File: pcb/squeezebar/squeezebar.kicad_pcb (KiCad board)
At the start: 2 copper layers, 104.1 x 20.3 mm, 55 parts, among them J2 Conn_02x08_Counter_Clockwise, U1 Elite-C

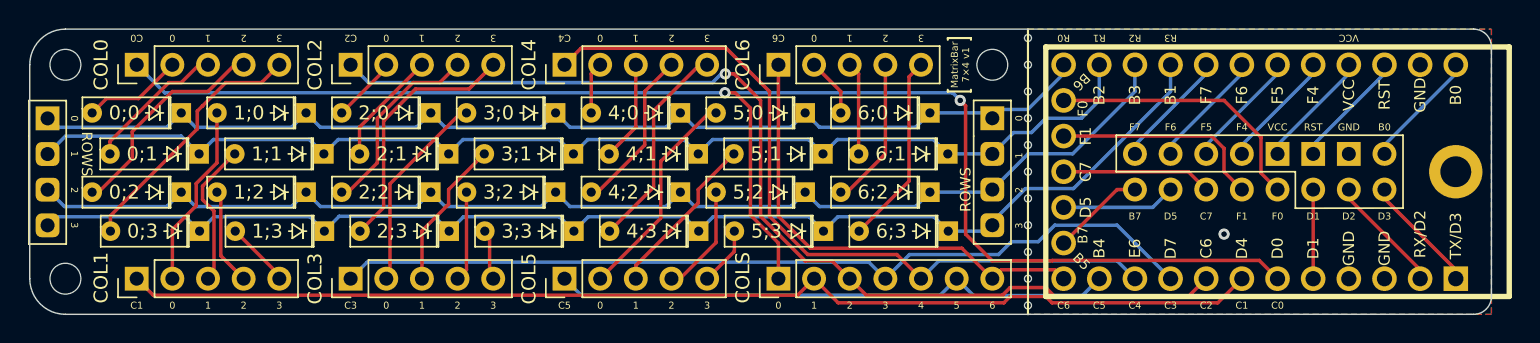
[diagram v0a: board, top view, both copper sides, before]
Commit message: Switch to M3 screws
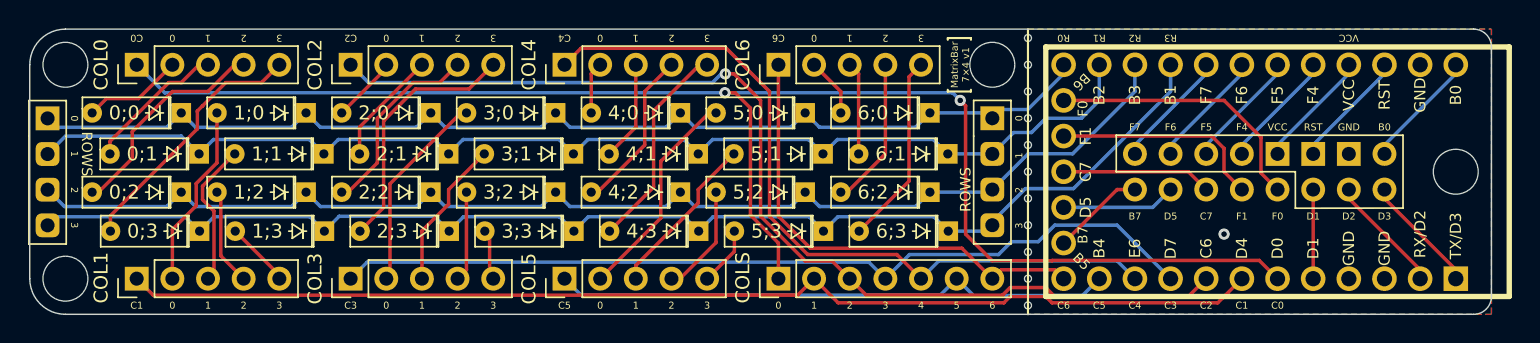
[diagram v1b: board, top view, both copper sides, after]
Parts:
- H1: footprint MountingHole:MountingHole_2.2mm_M2_DIN965_Pad -> MountingHole:MountingHole_3.2mm_M3_DIN965
- H2, H3, H4: footprint MountingHole:MountingHole_2.2mm_M2_DIN965 -> MountingHole:MountingHole_3.2mm_M3_DIN965
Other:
- board text added: "M3"
- board text removed: "M2"
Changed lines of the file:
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@@
   (net 54 "/pf1")
   (net 55 "/pf0")
-  (footprint "MountingHole:MountingHole_2.2mm_M2_DIN965" (layer "F.Cu")
+  (footprint "MountingHole:MountingHole_3.2mm_M3_DIN965" (layer "F.Cu")
     (at 30.48 60.96)
-    (descr "Mounting Hole 2.2mm, no annular, M2, DIN965")
-    (tags "mounting hole 2.2mm no annular m2 din965")
+    (descr "Mounting Hole 3.2mm, no annular, M3, DIN965")
+    (tags "mounting hole 3.2mm no annular m3 din965")
     (property "Sheetfile" "squeezebar.kicad_sch")
     (property "Sheetname" "")
     (attr exclude_from_pos_files)
-    (fp_text reference "H3" (at 0 -2.9) (layer "F.SilkS") hide
+    (fp_text reference "H3" (at 0 -3.8) (layer "F.SilkS") hide
       (effects (font (size 1 1) (thickness 0.15)))
     )
-    (fp_text value "MountingHole" (at 0 2.9) (layer "F.Fab")
+    (fp_text value "MountingHole" (at 0 3.8) (layer "F.Fab")
       (effects (font (size 1 1) (thickness 0.15)))
     )
@@
       (effects (font (size 1 1) (thickness 0.15)))
     )
-    (fp_circle (center 0 0) (end 1.9 0) (layer "Cmts.User") (width 0.15) (fill none))
-    (fp_circle (center 0 0) (end 2.15 0) (layer "F.CrtYd") (width 0.05) (fill none))
-    (pad "" np_thru_hole circle (at 0 0) (size 2.2 2.2) (drill 2.2) (layers *.Cu *.Mask))
+    (fp_circle (center 0 0) (end 2.8 0) (layer "Cmts.User") (width 0.15) (fill none))
+    (fp_circle (center 0 0) (end 3.05 0) (layer "F.CrtYd") (width 0.05) (fill none))
+    (pad "" np_thru_hole circle (at 0 0) (size 3.2 3.2) (drill 3.2) (layers *.Cu *.Mask))
   )
   (footprint "Library:breakaway-hole" (layer "F.Cu")
@@
       (net 26 "Net-(4;0-Pad2)") (pinfunction "A") (pintype "passive"))
   )
-  (footprint "MountingHole:MountingHole_2.2mm_M2_DIN965_Pad" (layer "F.Cu")
+  (footprint "MountingHole:MountingHole_3.2mm_M3_DIN965" (layer "F.Cu")
     (at 129.54 68.58)
-    (descr "Mounting Hole 2.2mm, M2, DIN965")
-    (tags "mounting hole 2.2mm m2 din965")
+    (descr "Mounting Hole 3.2mm, no annular, M3, DIN965")
+    (tags "mounting hole 3.2mm no annular m3 din965")
     (property "Sheetfile" "squeezebar.kicad_sch")
     (property "Sheetname" "")
     (attr exclude_from_pos_files)
-    (fp_text reference "H1" (at 0 -2.9) (layer "F.SilkS") hide
+    (fp_text reference "H1" (at 0 -3.8) (layer "F.SilkS") hide
       (effects (font (size 1 1) (thickness 0.15)))
     )
-    (fp_text value "MountingHole" (at 0 2.9) (layer "F.Fab")
+    (fp_text value "MountingHole" (at 0 3.8) (layer "F.Fab")
       (effects (font (size 1 1) (thickness 0.15)))
     )
@@
       (effects (font (size 1 1) (thickness 0.15)))
     )
-    (fp_circle (center 0 0) (end 1.9 0) (layer "Cmts.User") (width 0.15) (fill none))
-    (fp_circle (center 0 0) (end 2.15 0) (layer "F.CrtYd") (width 0.05) (fill none))
-    (pad "1" thru_hole circle (at 0 0) (size 3.8 3.8) (drill 2.2) (layers *.Cu *.Mask)
-      (net 40 "/gnd") (pinfunction "1") (pintype "input"))
+    (fp_circle (center 0 0) (end 2.8 0) (layer "Cmts.User") (width 0.15) (fill none))
+    (fp_circle (center 0 0) (end 3.05 0) (layer "F.CrtYd") (width 0.05) (fill none))
+    (pad "" np_thru_hole circle (at 0 0) (size 3.2 3.2) (drill 3.2) (layers *.Cu *.Mask))
   )
   (footprint "Library:PinHeader_1x05_P2.54mm_Vertical" (layer "F.Cu")
@@
       (net 5 "Net-(0;2-Pad2)") (pinfunction "A") (pintype "passive"))
   )
-  (footprint "MountingHole:MountingHole_2.2mm_M2_DIN965" (layer "F.Cu")
+  (footprint "MountingHole:MountingHole_3.2mm_M3_DIN965" (layer "F.Cu")
     (at 30.48 76.2)
-    (descr "Mounting Hole 2.2mm, no annular, M2, DIN965")
-    (tags "mounting hole 2.2mm no annular m2 din965")
+    (descr "Mounting Hole 3.2mm, no annular, M3, DIN965")
+    (tags "mounting hole 3.2mm no annular m3 din965")
     (property "Sheetfile" "squeezebar.kicad_sch")
     (property "Sheetname" "")
     (attr exclude_from_pos_files)
-    (fp_text reference "H4" (at 0 -2.9) (layer "F.SilkS") hide
+    (fp_text reference "H4" (at 0 -3.8) (layer "F.SilkS") hide
       (effects (font (size 1 1) (thickness 0.15)))
     )
-    (fp_text value "MountingHole" (at 0 2.9) (layer "F.Fab")
+    (fp_text value "MountingHole" (at 0 3.8) (layer "F.Fab")
       (effects (font (size 1 1) (thickness 0.15)))
     )
@@
       (effects (font (size 1 1) (thickness 0.15)))
     )
-    (fp_circle (center 0 0) (end 1.9 0) (layer "Cmts.User") (width 0.15) (fill none))
-    (fp_circle (center 0 0) (end 2.15 0) (layer "F.CrtYd") (width 0.05) (fill none))
-    (pad "" np_thru_hole circle (at 0 0) (size 2.2 2.2) (drill 2.2) (layers *.Cu *.Mask))
+    (fp_circle (center 0 0) (end 2.8 0) (layer "Cmts.User") (width 0.15) (fill none))
+    (fp_circle (center 0 0) (end 3.05 0) (layer "F.CrtYd") (width 0.05) (fill none))
+    (pad "" np_thru_hole circle (at 0 0) (size 3.2 3.2) (drill 3.2) (layers *.Cu *.Mask))
   )
   (footprint "Library:breakaway-hole" (layer "F.Cu")
@@
     )
   )
-  (footprint "MountingHole:MountingHole_2.2mm_M2_DIN965" (layer "F.Cu")
+  (footprint "MountingHole:MountingHole_3.2mm_M3_DIN965" (layer "F.Cu")
     (at 96.52 60.96)
-    (descr "Mounting Hole 2.2mm, no annular, M2, DIN965")
-    (tags "mounting hole 2.2mm no annular m2 din965")
+    (descr "Mounting Hole 3.2mm, no annular, M3, DIN965")
+    (tags "mounting hole 3.2mm no annular m3 din965")
     (property "Sheetfile" "squeezebar.kicad_sch")
     (property "Sheetname" "")
     (attr exclude_from_pos_files)
-    (fp_text reference "H2" (at 0 -2.9) (layer "F.SilkS") hide
+    (fp_text reference "H2" (at 0 -3.8) (layer "F.SilkS") hide
       (effects (font (size 1 1) (thickness 0.15)))
     )
-    (fp_text value "MountingHole" (at 0 2.9) (layer "F.Fab")
+    (fp_text value "MountingHole" (at 0 3.8) (layer "F.Fab")
       (effects (font (size 1 1) (thickness 0.15)))
     )
@@
       (effects (font (size 1 1) (thickness 0.15)))
     )
-    (fp_circle (center 0 0) (end 1.9 0) (layer "Cmts.User") (width 0.15) (fill none))
-    (fp_circle (center 0 0) (end 2.15 0) (layer "F.CrtYd") (width 0.05) (fill none))
-    (pad "" np_thru_hole circle (at 0 0) (size 2.2 2.2) (drill 2.2) (layers *.Cu *.Mask))
+    (fp_circle (center 0 0) (end 2.8 0) (layer "Cmts.User") (width 0.15) (fill none))
+    (fp_circle (center 0 0) (end 3.05 0) (layer "F.CrtYd") (width 0.05) (fill none))
+    (pad "" np_thru_hole circle (at 0 0) (size 3.2 3.2) (drill 3.2) (layers *.Cu *.Mask))
   )
   (footprint "Library:Diode" (layer "F.Cu")
@@
     (effects (font (size 0.5 0.5) (thickness 0.125)) (justify mirror))
   )
-  (gr_text "M2" (at 29.21 77.47 315) (layer "B.SilkS")
+  (gr_text "M3" (at 29.083 77.597 315) (layer "B.SilkS")
     (effects (font (size 0.5 0.5) (thickness 0.125)) (justify mirror))
   )
@@
     (effects (font (size 0.5 0.5) (thickness 0.125)))
   )
-  (dimension (type aligned) (layer "B.SilkS")
-    (pts (xy 30.48 76.2) (xy 27.94 76.2))
-    (height 1.27)
-    (gr_text "2.54" (at 29.21 74.93) (layer "B.SilkS")
-      (effects (font (size 0.5 0.5) (thickness 0.15)) (justify mirror))
-    )
-    (format (units 3) (units_format 0) (precision 2))
-    (style (thickness 0.15) (arrow_length 0.4) (text_position_mode 1) (extension_height 0.58642) (extension_offset 0.5) keep_text_aligned)
-  )
-  (dimension (type aligned) (layer "B.SilkS")
-    (pts (xy 30.48 76.2) (xy 30.48 78.74))
-    (height -1.27)
-    (gr_text "2.54" (at 31.75 77.47 90) (layer "B.SilkS")
-      (effects (font (size 0.5 0.5) (thickness 0.15)) (justify mirror))
-    )
-    (format (units 3) (units_format 0) (precision 2))
-    (style (thickness 0.15) (arrow_length 0.3) (text_position_mode 1) (extension_height 0.58642) (extension_offset 0.5) keep_text_aligned)
-  )
   (dimension (type aligned) (layer "Cmts.User")
     (pts (xy 27.88 66.05) (xy 134.874 66.04))
@@
   )
   (dimension (type aligned) (layer "User.1")
-    (pts (xy 129.54 68.58) (xy 129.54 66.548))
-    (height 7.62)
-    (gr_text "2 mm" (at 137.16 64.0334 90) (layer "User.1")
-      (effects (font (size 1 1) (thickness 0.15)))
-    )
-    (format (units 3) (units_format 1) (precision 1) suppress_zeroes)
-    (style (thickness 0.15) (arrow_length 1) (text_position_mode 2) (extension_height 0.58642) (extension_offset 0.5) keep_text_aligned)
-  )
-  (dimension (type aligned) (layer "User.1")
-    (pts (xy 27.94 78.74) (xy 97.155 78.74))
+    (pts (xy 27.94 78.74) (xy 96.52 78.74))
     (height 6.35)
-    (gr_text "69.22 mm" (at 62.5475 85.09) (layer "User.1")
+    (gr_text "68.58 mm" (at 62.23 85.09) (layer "User.1")
       (effects (font (size 1 1) (thickness 0.15)))
     )
@@
   )
   (dimension (type aligned) (layer "User.1")
-    (pts (xy 97.155 78.74) (xy 134.62 78.74))
+    (pts (xy 96.52 78.74) (xy 134.62 78.74))
     (height 6.35)
-    (gr_text "37.47 mm" (at 115.8875 85.09) (layer "User.1")
+    (gr_text "38.10 mm" (at 115.57 85.09) (layer "User.1")
       (effects (font (size 1 1) (thickness 0.15)))
     )

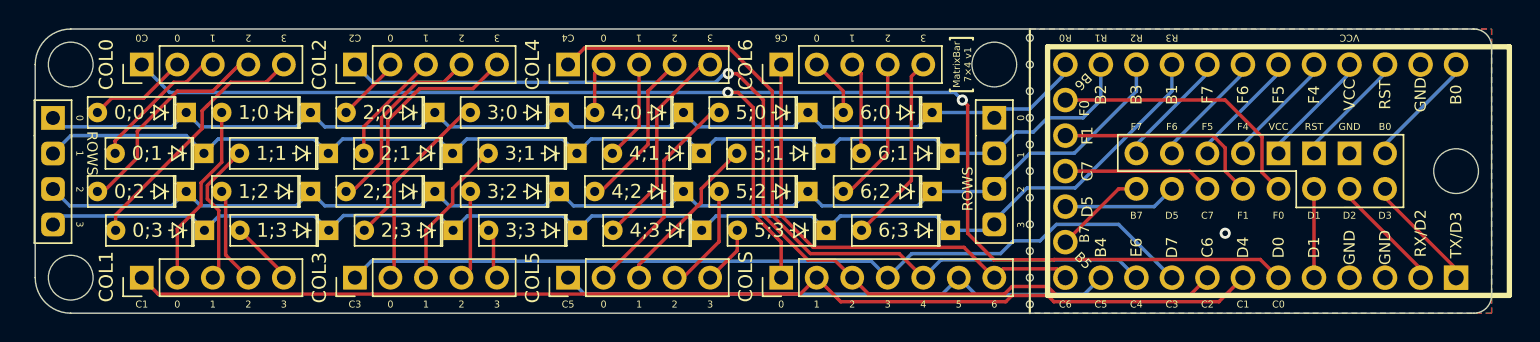
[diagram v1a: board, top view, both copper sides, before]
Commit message: Reassign pins; break out I²C & RST at the expense of 2 mounting holes
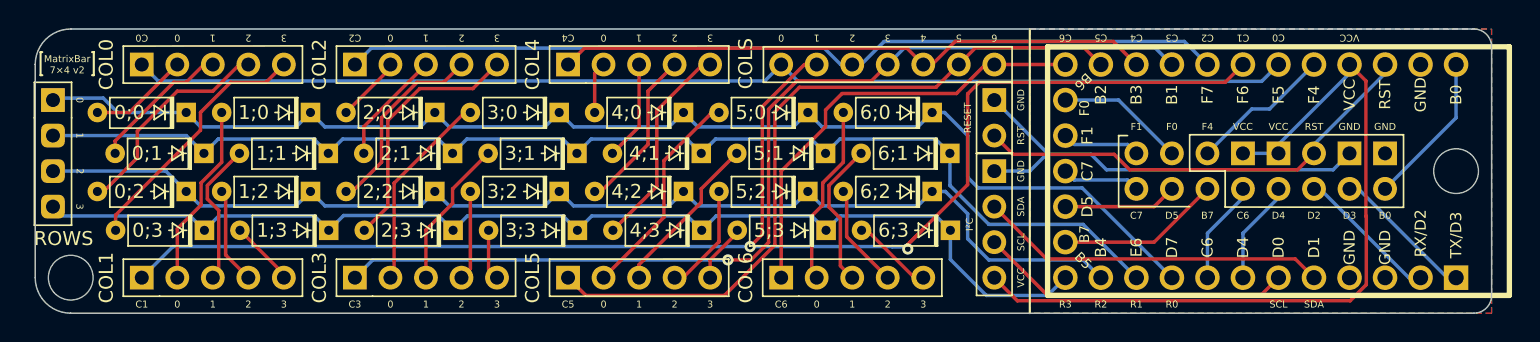
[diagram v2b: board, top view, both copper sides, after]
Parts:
- removed H2, H3: MountingHole, MountingHole:MountingHole_3.2mm_M3_DIN965
- removed REF** (x11): breakaway-hole, Library:breakaway-hole
- removed ROWS1: PINSOCKET, Library:PinSocket_1x04_P2.54mm_Vertical_LongPads
- added J1: RESET, Library:PinHeader_RST_1x02_P2.54mm_Vertical, B.Cu at (96.5, 63.5)
- added J3: I2C, Library:PinHeader_I2C_1x04_P2.54mm_Vertical, F.Cu at (96.5, 68.6)
- COL0, COL1, COL2, COL3, COL4, COL5, COL6: footprint Library:PinHeader_1x05_P2.54mm_Vertical -> Library:PinHeader_Col_1x05_P2.54mm_Vertical
- COLUMNS1: footprint Connector_PinHeader_2.54mm:PinHeader_1x07_P2.54mm_Vertical -> Library:PinHeader_COLS_1x07_P2.54mm_Vertical
- moved COL6 15.2 mm to (81.3, 76.2)
- moved COLUMNS1 15.2 mm to (81.3, 61.0)
- moved ROWS2 1.28 mm to (29.2, 63.5)
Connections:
- J2 pad 1: /pd3 -> /pb0
- J2 pad 10: /pf4 -> /vcc
- J2 pad 11: /pc7 -> /pb7
- J2 pad 12: /pf5 -> /pf4
- J2 pad 14: /pf6 -> /pf0
- J2 pad 15: /pb7 -> /pc7
- J2 pad 16: /pf7 -> /pf1
- J2 pad 2: /pb0 -> /gnd
- J2 pad 3: /pd2 -> /pd3
- J2 pad 5: /pd1 -> /pd2
- J2 pad 7: /pf0 -> /pd4
- J2 pad 9: /pf1 -> /pc6
- U1 pad 10: /c4 -> /r1
- U1 pad 11: /c5 -> /r2
- U1 pad 12: /c6 -> /r3
- U1 pad 13: /r0 -> /c6
- U1 pad 14: /r1 -> /c5
- U1 pad 15: /r2 -> /c4
- U1 pad 16: /r3 -> /c3
- U1 pad 17: /pf7 -> /c2
- U1 pad 18: /pf6 -> /c1
- U1 pad 19: /pf5 -> /c0
- U1 pad 5: /pd1 -> /sda
- U1 pad 6: /c0 -> /scl
- U1 pad 7: /c1 -> /pd4
- U1 pad 8: /c2 -> /pc6
- U1 pad 9: /c3 -> /r0
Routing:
- net /vcc: track 7.18 -> 53.7 mm
- net /gnd: track 0.00 -> 32.3 mm, vias 1 -> 0
- net /c1: track 81.5 -> 106.9 mm, vias 0 -> 2
- net /c0: track 108.2 -> 83.2 mm, vias 2 -> 0
- net /sda: track 0.00 -> 25.0 mm
- net /rst: track 7.18 -> 31.5 mm
- net /scl: track 0.00 -> 22.4 mm
- net /r0: track 77.3 -> 92.0 mm
- net /c5: track 40.1 -> 52.0 mm
- net /c4: track 54.2 -> 42.3 mm
- net /c2: track 74.1 -> 62.7 mm, vias 1 -> 0
- net /pf0: track 19.4 -> 9.20 mm
- net /pf1: track 15.3 -> 5.61 mm
- net /r3: track 90.3 -> 81.0 mm
- net Net-(6;3-Pad2): track 13.7 -> 4.79 mm
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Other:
- board text added: "D4"
- board text added: "I²C"
- board text added: "MatrixBar 7×4 v2"
- board text added: "RESET"
- board text added: "SCL"
- board text added: "SDA"
- board text removed: "D1"
- board text removed: "F5"
- board text removed: "F6"
- board text removed: "F7"
- board text removed: "MatrixBar 7×4 v1"

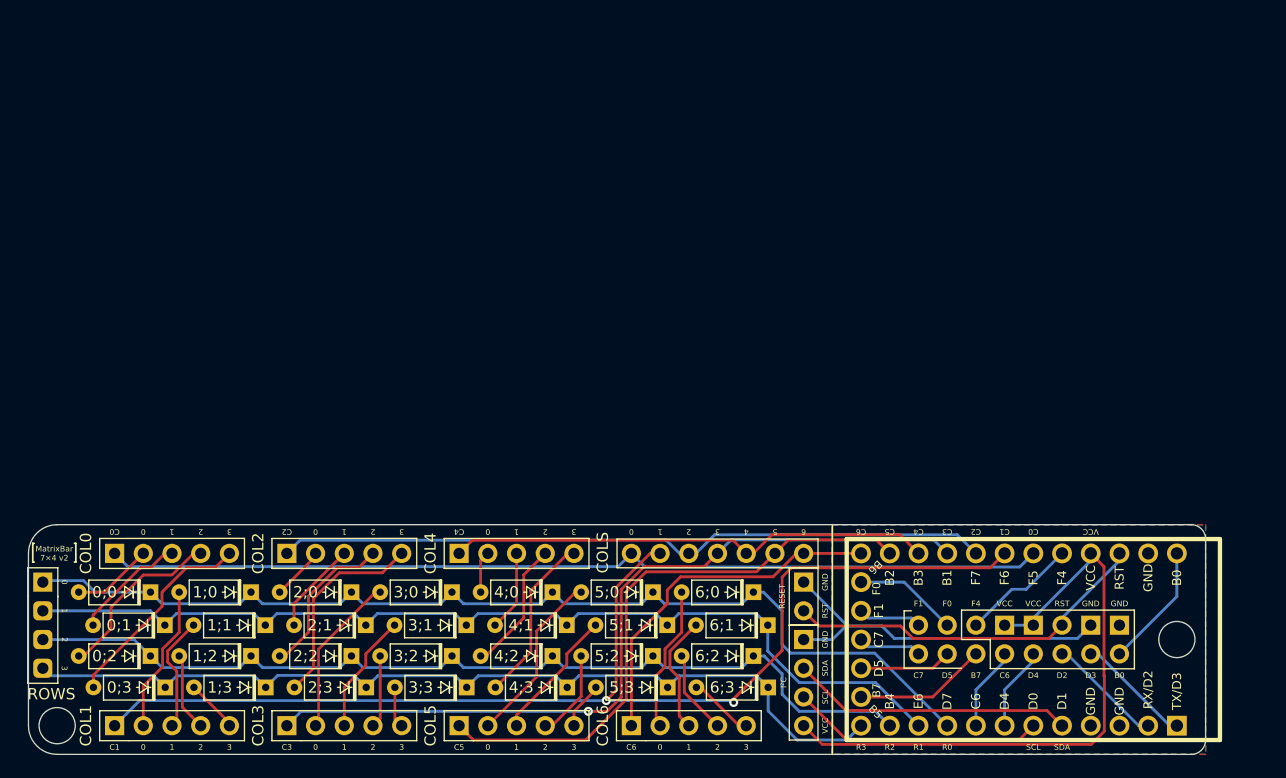
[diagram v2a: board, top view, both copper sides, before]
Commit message: Move mounting hole from under the MCU
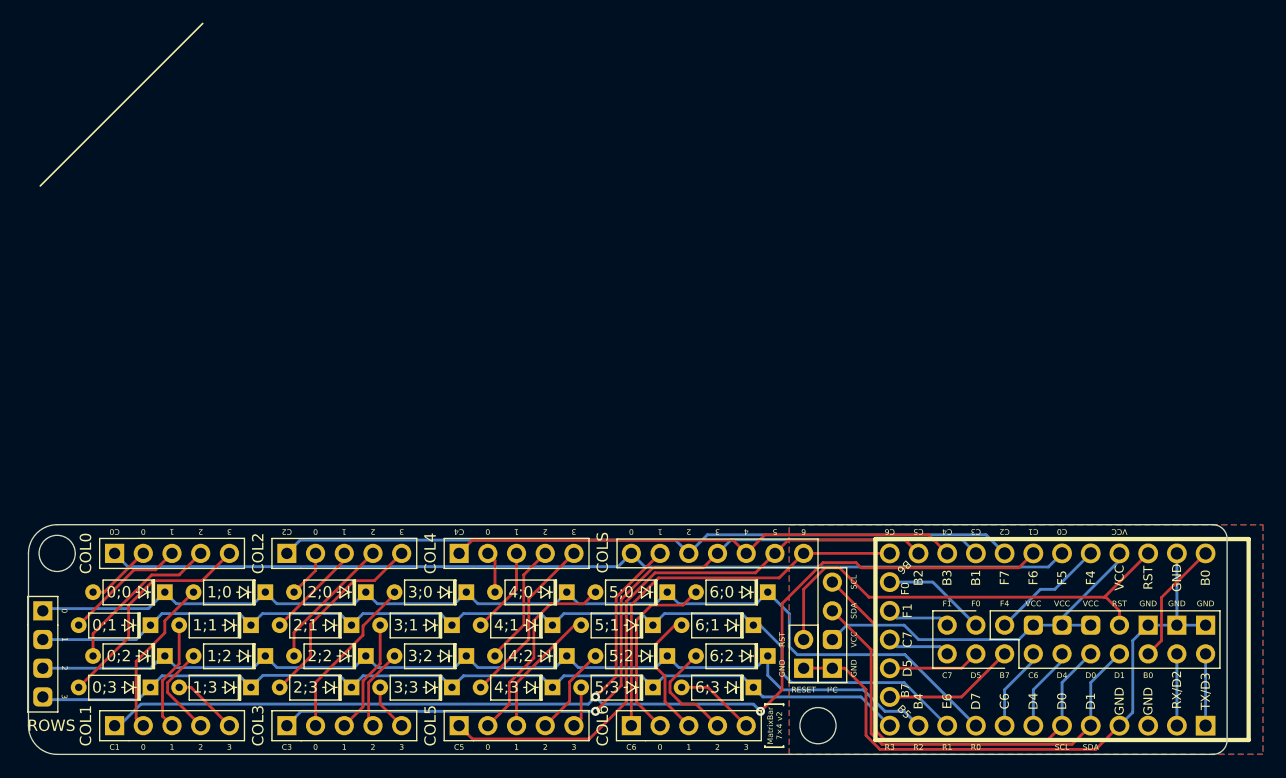
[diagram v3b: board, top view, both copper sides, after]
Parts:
- removed H1: MountingHole, MountingHole:MountingHole_3.2mm_M3_DIN965
- added H2: MountingHole, MountingHole:MountingHole_3.2mm_M3_DIN965, F.Cu at (97.8, 76.2)
- J1: moved to F.Cu
- J2: footprint Library:PinSocket_2x08_P2.54mm_Bespoke -> Library:PinSocket_2x10_P2.54mm_Bespoke
- J3: moved to B.Cu
- moved H4 15.2 mm to (30.5, 61.0)
- moved J2 7.62 mm to (132.1, 69.8)
- moved J1 7.62 mm to (96.5, 71.1)
- moved J3 3.59 mm to (99.1, 71.1)
- moved ROWS2 2.54 mm to (29.2, 66.0)
- moved U1 2.54 mm to (118.1, 68.6)
- moved 0;3 1.30 mm to (38.7, 72.8)
- moved 1;3 1.30 mm to (47.6, 72.8)
- moved 2;3 1.30 mm to (56.5, 72.8)
- moved 3;3 1.30 mm to (65.4, 72.8)
- moved 4;3 1.30 mm to (74.3, 72.8)
- moved 5;3 1.30 mm to (83.2, 72.8)
- moved 6;3 1.30 mm to (92.1, 72.8)
- moved 0;0 1.27 mm to (40.0, 64.4)
- moved 0;1 1.27 mm to (38.7, 67.3)
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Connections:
- J2 pad 1: /pb0 -> /pd3
- J2 pad 11: /pb7 -> /pd4
- J2 pad 12: /pf4 -> /vcc
- J2 pad 13: /pd5 -> /pc6
- J2 pad 14: /pf0 -> /vcc
- J2 pad 15: /pc7 -> /pb7
- J2 pad 16: /pf1 -> /pf4
- J2 pad 3: /pd3 -> /pd2
- J2 pad 5: /pd2 -> /pb0
- J2 pad 6: /rst -> /gnd
- J2 pad 7: /pd4 -> /sda
- J2 pad 8: /vcc -> /rst
- J2 pad 9: /pc6 -> /scl
- J3 pad 2: /sda -> /vcc
- J3 pad 3: /scl -> /sda
- J3 pad 4: /vcc -> /scl
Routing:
- net /gnd: track 32.3 -> 55.5 mm
- net /vcc: track 53.7 -> 31.6 mm
- net /scl: track 22.4 -> 39.4 mm
- net /sda: track 25.0 -> 40.2 mm
- net /rst: track 31.5 -> 41.5 mm
- net /c6: track 31.2 -> 35.4 mm
- net Net-(6;0-Pad2): track 12.4 -> 16.5 mm
- net /pd2: track 9.82 -> 6.35 mm
- net /c2: track 62.7 -> 65.8 mm
- net /c4: track 42.3 -> 45.5 mm
- net Net-(5;0-Pad2): track 15.5 -> 18.2 mm
- net /pd3: track 8.98 -> 6.35 mm
- net /r0: track 92.0 -> 94.6 mm
- net /r1: track 88.1 -> 90.7 mm
- net /c0: track 83.2 -> 85.8 mm
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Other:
- board size 104.1 x 20.3 mm -> 106 x 20.3 mm
- board text added: "D0"
- board text added: "D1"
- board text removed: "D2"
- board text removed: "D3"
